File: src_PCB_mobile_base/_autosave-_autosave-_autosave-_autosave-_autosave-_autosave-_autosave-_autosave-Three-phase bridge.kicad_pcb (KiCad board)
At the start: 2 copper layers, 401.6 x 318 mm, 105 parts, among them M1 MCP6022-I/P, M2 MCP6022-I/P, P1 CONN_1, P10 CONN_1, P11 CONN_1, P12 CONN_1, P13 CONN_1, P2 POWER_FUSE, P3 CONN_2, P4 CONN_1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

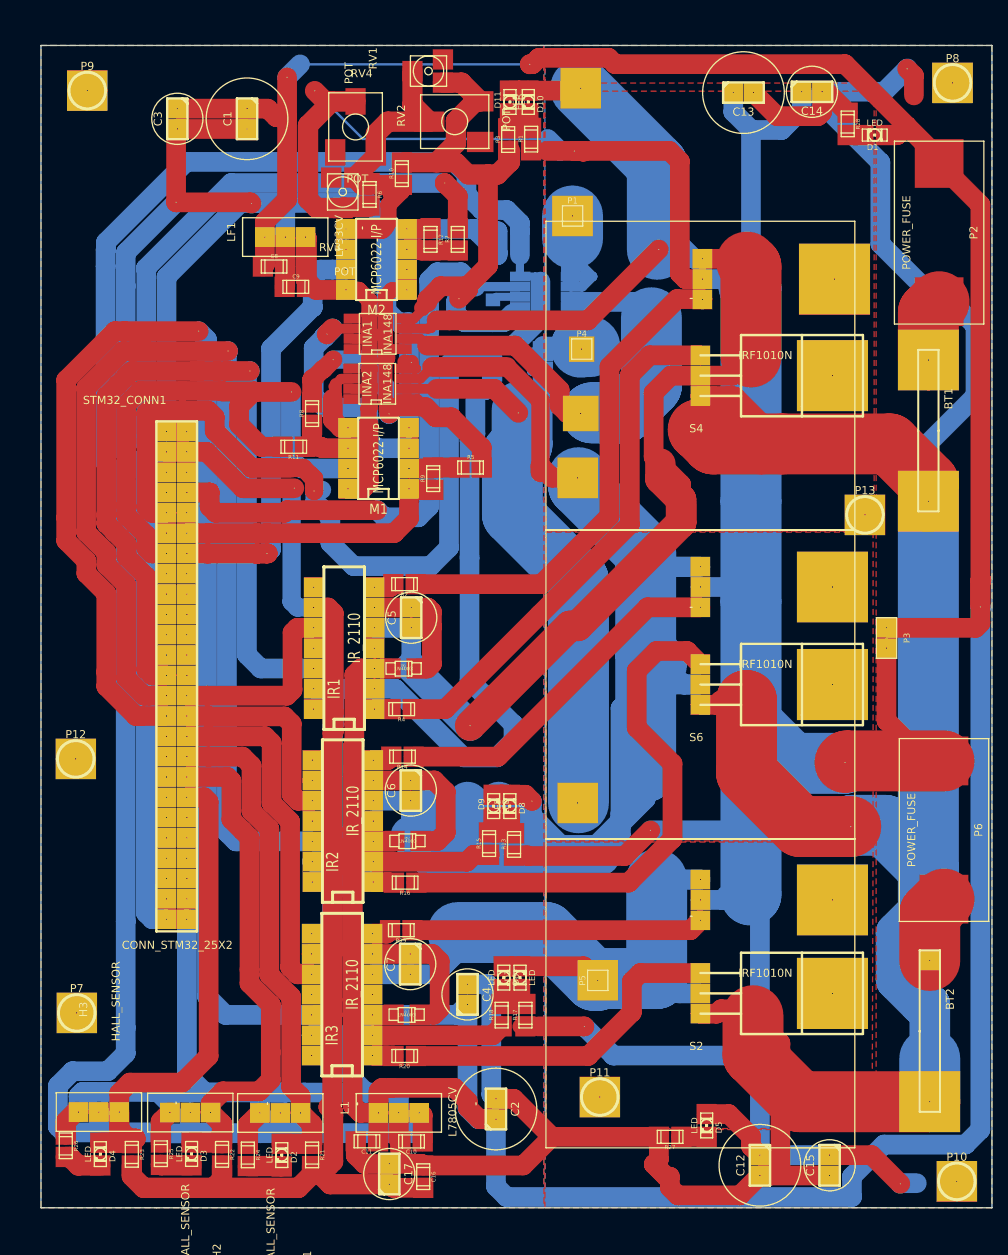
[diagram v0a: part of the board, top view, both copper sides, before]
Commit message: Modulos originales de libreria de Sebastian
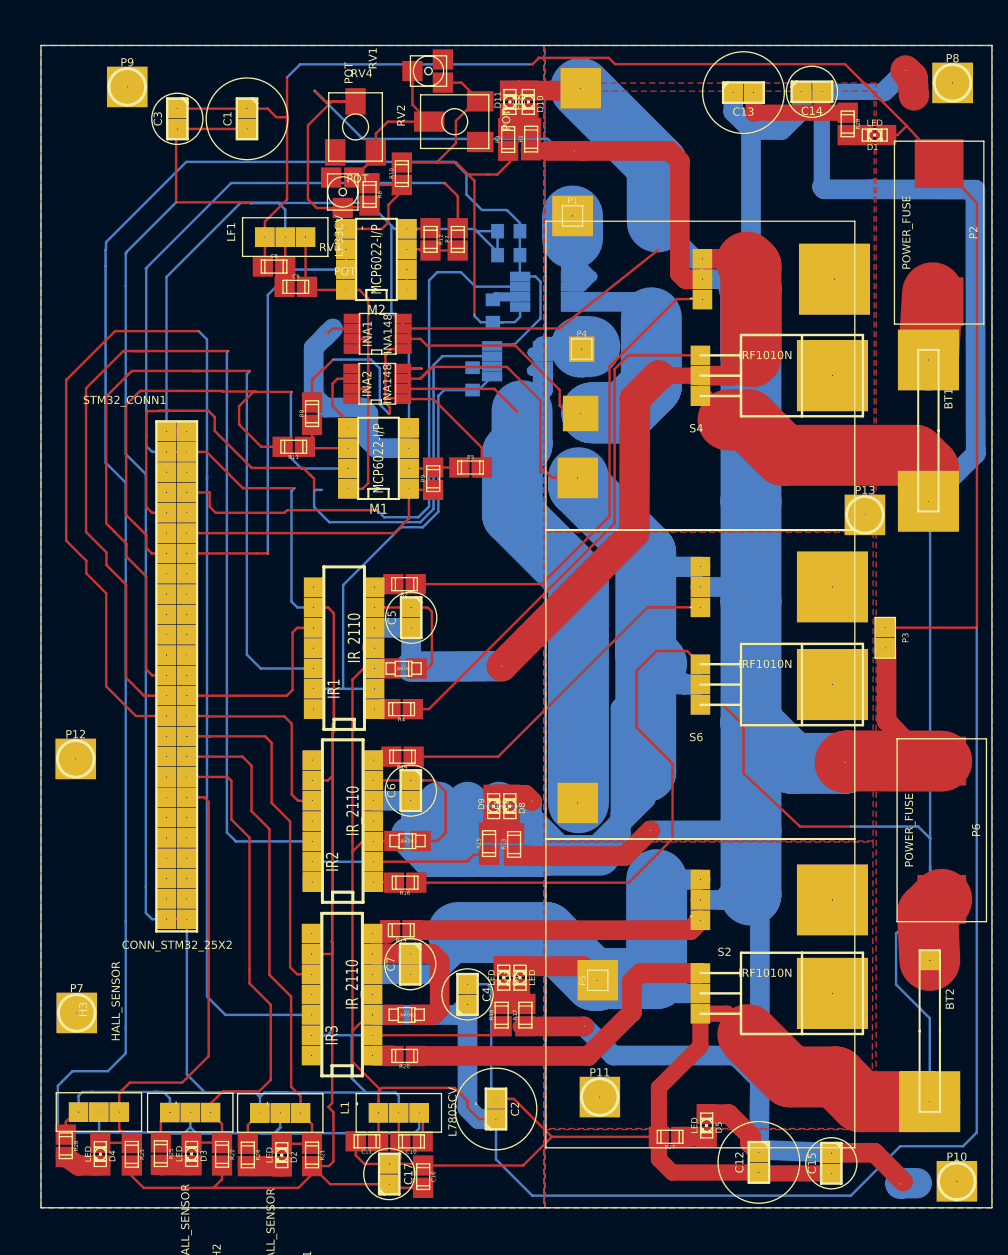
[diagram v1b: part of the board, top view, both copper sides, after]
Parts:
- moved P9 5.01 mm to (167.8, 69.7)
- moved C12 0.39 mm to (246.7, 204.1)
- moved C15 0.33 mm to (255.8, 204.2)
- moved P6 0.28 mm to (269.6, 162.6)
- moved P3 0.16 mm to (262.5, 138.6)
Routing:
- net VCC: track 499.6 -> 457.5 mm
- net GND: track 1061.5 -> 1020.6 mm
- net N-0000074: track 201.6 -> 174.6 mm
- net N-00000100: track 70.8 -> 49.1 mm
- net +3.3V: track 59.0 -> 44.9 mm
- net N-0000088: track 98.6 -> 89.3 mm
- net N-0000084: track 4.75 -> 2.51 mm
- net N-0000020: track 11.1 -> 9.00 mm
- net +48V: track 408.2 -> 409.2 mm
- net N-0000014: track 7.85 -> 8.43 mm
- net N-000008: track 55.8 -> 56.3 mm
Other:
- net class 12 mil removed
- net class pista12mm added: clearance 0.254, trace_width 0.3048, via_dia 0.127, via_drill 0.1016
